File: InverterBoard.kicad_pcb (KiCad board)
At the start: 2 copper layers, 72 x 95 mm, 109 parts, among them J1 PinHeader, J2 5VIN, J3 GateDrivePower, J4 Motor, J5 BrakeResistor, J6 DC_Link, Q1 IPA60R280P7S, Q2 IPA60R280P7S, Q3 IPA60R280P7S, Q4 IPA60R280P7S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

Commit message: アートワークも一応完成
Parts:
- removed the R23 at (-88.9, -2.54)
- removed the R24 at (-85.1, 29.2)
- removed the R24 at (-83.8, 21.6)
- removed the REF** at (33.0, 44.5)
- removed the REF** at (-33.0, 44.5)
- removed the REF** at (33.0, -44.5)
- added R24: 330R, Resistor_SMD:R_0603_1608Metric, B.Cu at (21.0, 19.1)
- added REF**: MountingHole_3.2mm_M3, MountingHole:MountingHole_3.2mm_M3, F.Cu at (44.5, -33.0)
- added REF**: MountingHole_3.2mm_M3, MountingHole:MountingHole_3.2mm_M3, F.Cu at (44.5, 33.0)
- added REF**: MountingHole_3.2mm_M3, MountingHole:MountingHole_3.2mm_M3, F.Cu at (-44.5, -33.0)
- C16, C17, C18, C19, C20, C21, JP1, JP2, R23, R25, R26, R27, R28: moved to B.Cu
- moved C17 127.0 mm to (25.4, 21.0)
- moved R27 123.3 mm to (29.2, 23.5), turned to 90 degrees
- moved C21 122.6 mm to (31.1, 20.3), turned to 90 degrees
- moved R28 119.5 mm to (29.2, 20.3), turned to 90 degrees
- moved JP2 101.7 mm to (25.4, 23.1)
- moved C19 98.6 mm to (21.0, 21.0), turned to 180 degrees
- moved C16 98.1 mm to (-5.08, 26.0)
- moved C1 96.8 mm to (-29.8, 33.0), turned to 270 degrees
- moved JP1 95.4 mm to (-5.08, 28.2)
- moved R23 95.0 mm to (-0.64, 24.1), turned to 180 degrees
- moved R25 89.2 mm to (-6.99, 30.2)
- moved C18 86.8 mm to (-0.64, 26.0), turned to 180 degrees
- moved C20 84.7 mm to (-3.17, 31.8)
- moved D4 84.2 mm to (-27.9, 29.8)
- moved C2 82.1 mm to (-23.5, 33.0), turned to 270 degrees
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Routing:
- net GND: track 2.78 -> 181.4 mm, vias 1 -> 7
- net GNDPWR: track 222.6 -> 401.0 mm, vias 3 -> 6
- net +3V3: track 2.78 -> 124.2 mm, vias 1 -> 2
- net /Sensor/IW-: track 39.8 -> 104.2 mm, vias 1 -> 4
- net /Sensor/IU-: track 44.8 -> 106.1 mm, vias 1 -> 4
- net /GateDrive/GATE_WP: track 0.00 -> 54.8 mm, vias 0 -> 1
- net /GateDrive/GATE_VP: track 0.00 -> 52.4 mm, vias 0 -> 1
- net SIG_BR: track 0.00 -> 51.4 mm
- net /GateDrive/GATE_UP: track 0.00 -> 48.8 mm, vias 0 -> 1
- net /GateDrive/SOURCE_VP: track 67.7 -> 114.3 mm, vias 0 -> 3
- net /GateDrive/GATE_WN: track 0.00 -> 43.5 mm, vias 0 -> 1
- net /GateDrive/GATE_VN: track 0.00 -> 40.7 mm, vias 0 -> 1
- net /GateDrive/GATE_UN: track 0.00 -> 39.1 mm, vias 0 -> 1
- net SEN_IU_REF: track 0.00 -> 38.8 mm
- net SIG_UP: track 0.00 -> 38.5 mm
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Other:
- board size 72 x 95 mm -> 95 x 72 mm
- board text added: "-"
- board text added: "1"
- board text added: "19"
- board text added: "2"
- board text added: "20"
- board text added: "Designed by @akito_0914"
- board text added: "GBR"
- board text added: "GND"
- board text added: "GUN"
- board text added: "GUP"
- board text added: "GVN"
- board text added: "GVP"
- board text added: "GWN"
- board text added: "GWP"
- board text added: "Inverter board"
- board text added: "MOTOR"
- board text added: "MyServoAmpProject"
- board text added: "RES"
- board text added: "SIU"
- board text added: "SIU0"
- board text added: "SIW"
- board text added: "SIW0"
- board text added: "SVDC+"
- board text added: "SVDC-"
- board text added: "VDC"

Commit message: TODO削除
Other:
- board text removed: "TODO: Fix connection from motor line to current sensor."
- board text removed: "TODO: Fix via at current sensor."
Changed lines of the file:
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@@
   (general
     (thickness 1.6)
-    (drawings 121)
+    (drawings 119)
     (tracks 769)
     (zones 0)
@@
   )
   (setup
-    (last_trace_width 1)
+    (last_trace_width 0.25)
     (user_trace_width 0.15)
     (user_trace_width 0.2)
@@
     (arrow2b (pts (xy 0 45.72) (xy 1.126504 45.133579)))
   )
-  (gr_text "TODO: Fix connection from motor line to current sensor." (at 327.66 -109.22) (layer Dwgs.User)
-    (effects (font (size 10 10) (thickness 1.5)))
-  )
-  (gr_text "TODO: Fix via at current sensor." (at 232.41 -128.905) (layer Dwgs.User)
-    (effects (font (size 10 10) (thickness 1.5)))
-  )
   (gr_line (start -27.94 20.32) (end 11.43 20.32) (layer Dwgs.User) (width 0.15))

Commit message: テストポイント追加，シルク調整，固定穴マスク追加
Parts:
- removed REF** (x4): MountingHole_3.2mm_M3, MountingHole:MountingHole_3.2mm_M3
- added H1: MountingHole, MountingHole:MountingHole_3.2mm_M3, F.Cu at (-44.5, -33.0)
- added H2: MountingHole, MountingHole:MountingHole_3.2mm_M3, F.Cu at (44.5, -33.0)
- added H3: MountingHole, MountingHole:MountingHole_3.2mm_M3, F.Cu at (44.5, 33.0)
- added H4: MountingHole, MountingHole:MountingHole_3.2mm_M3, F.Cu at (-44.5, 33.0)
- added TP1: TestPoint, TestPoint:TestPoint_Loop_D2.50mm_Drill1.0mm_LowProfile, F.Cu at (-41.9, 27.9)
- added TP10: TestPoint, TestPoint:TestPoint_Pad_D1.0mm, F.Cu at (-5.08, 27.3)
- added TP11: TestPoint, TestPoint:TestPoint_Pad_D1.0mm, F.Cu at (0.00, 27.3)
- added TP12: TestPoint, TestPoint:TestPoint_Pad_D1.0mm, F.Cu at (5.08, 27.3)
- added TP13: TestPoint, TestPoint:TestPoint_Loop_D2.50mm_Drill1.0mm_LowProfile, F.Cu at (-33.0, -29.8)
- added TP14: TestPoint, TestPoint:TestPoint_Loop_D2.50mm_Drill1.0mm_LowProfile, F.Cu at (-38.7, -33.0)
- added TP15: TestPoint, TestPoint:TestPoint_Loop_D2.50mm_Drill1.0mm_LowProfile, F.Cu at (-28.6, -5.71)
- added TP16: TestPoint, TestPoint:TestPoint_Loop_D2.50mm_Drill1.0mm_LowProfile, F.Cu at (-5.08, -9.50)
- added TP17: TestPoint, TestPoint:TestPoint_Loop_D2.50mm_Drill1.0mm_LowProfile, F.Cu at (10.2, -9.53)
- added TP18: TestPoint, TestPoint:TestPoint_Loop_D2.50mm_Drill1.0mm_LowProfile, F.Cu at (25.4, -9.50)
- added TP19: TestPoint, TestPoint:TestPoint_Pad_D1.0mm, B.Cu at (0.00, 27.9)
- added TP2: TestPoint, TestPoint:TestPoint_Loop_D2.50mm_Drill1.0mm_LowProfile, F.Cu at (-19.7, 33.0)
- added TP20: TestPoint, TestPoint:TestPoint_Pad_D1.0mm, B.Cu at (21.6, 22.9)
- added TP21: TestPoint, TestPoint:TestPoint_Pad_D1.0mm, B.Cu at (-5.71, 32.4)
- added TP22: TestPoint, TestPoint:TestPoint_Pad_D1.0mm, B.Cu at (31.8, 22.9)
- added TP23: TestPoint, TestPoint:TestPoint_Pad_D1.0mm, F.Cu at (45.7, 8.89)
- added TP24: TestPoint, TestPoint:TestPoint_Loop_D2.50mm_Drill1.0mm_LowProfile, F.Cu at (36.8, 12.1)
- added TP25: TestPoint, TestPoint:TestPoint_Pad_D1.0mm, F.Cu at (37.5, 23.5)
- added TP26: TestPoint, TestPoint:TestPoint_Pad_D1.0mm, F.Cu at (37.5, 20.3)
- added TP3: TestPoint, TestPoint:TestPoint_Loop_D2.50mm_Drill1.0mm_LowProfile, F.Cu at (-45.1, 24.8)
- added TP4: TestPoint, TestPoint:TestPoint_Loop_D2.50mm_Drill1.0mm_LowProfile, F.Cu at (-36.8, 12.1)
- added TP5: TestPoint, TestPoint:TestPoint_Pad_D1.0mm, F.Cu at (45.7, -1.91)
- added TP6: TestPoint, TestPoint:TestPoint_Pad_D1.0mm, F.Cu at (-20.3, 27.3)
- added TP7: TestPoint, TestPoint:TestPoint_Pad_D1.0mm, F.Cu at (-15.2, 27.3)
- added TP8: TestPoint, TestPoint:TestPoint_Pad_D1.0mm, F.Cu at (-25.4, 27.3)
- added TP9: TestPoint, TestPoint:TestPoint_Pad_D1.0mm, F.Cu at (-10.2, 27.3)
- C24: moved to F.Cu
- C25, R41, R42: moved to B.Cu
- J1: footprint Connector_PinHeader_2.54mm:PinHeader_2x10_P2.54mm_Vertical -> Connector_IDC:IDC-Header_2x10_P2.54mm_Vertical
- moved D1 7.41 mm to (-22.2, 29.8), turned to 90 degrees
- moved R1 6.87 mm to (-24.8, 29.8)
- moved R41 3.86 mm to (36.2, 26.7), turned to 270 degrees
- moved D2 3.18 mm to (-33.0, 14.0)
- moved C7 2.54 mm to (-27.9, 16.3)
- moved D7 2.54 mm to (-27.9, 11.7)
- moved R11 2.54 mm to (-27.9, 26.9)
- moved R14 2.54 mm to (-27.9, 14.6)
- moved R3 2.54 mm to (-23.5, -33.0)
- moved U4 2.54 mm to (-27.9, 21.6)
- moved C6 2.54 mm to (-17.8, 16.3)
- moved D8 2.54 mm to (-17.8, 11.7)
- moved R10 2.54 mm to (-17.8, 26.9)
- moved R13 2.54 mm to (-17.8, 14.6)
- moved U3 2.54 mm to (-17.8, 21.6)
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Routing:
- net GNDPWR: track 401.0 -> 422.5 mm
- net GND: track 181.4 -> 199.9 mm, vias 7 -> 9
- net /Sensor/IW-: track 104.2 -> 116.5 mm
- net /Sensor/IU-: track 106.1 -> 117.0 mm
- net SEN_VDC_N: track 8.78 -> 18.6 mm, vias 0 -> 1
- net +5VP: track 6.43 -> 15.7 mm
- net Net-(C22-Pad1): track 12.7 -> 20.5 mm
- net /GateDrive/GATE_WP: track 54.8 -> 61.0 mm
- net Net-(R41-Pad2): track 6.85 -> 13.0 mm, vias 0 -> 1
- net /GateDrive/SOURCE_VP: track 114.3 -> 120.1 mm
- net SEN_VDC_P: track 10.7 -> 16.0 mm, vias 0 -> 1
- net /MainCircuit/BR_L: track 32.9 -> 38.1 mm
- net SIG_VN: track 26.1 -> 31.1 mm
- net SIG_VP: track 33.6 -> 38.5 mm
- net SIG_WP: track 24.9 -> 29.8 mm
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
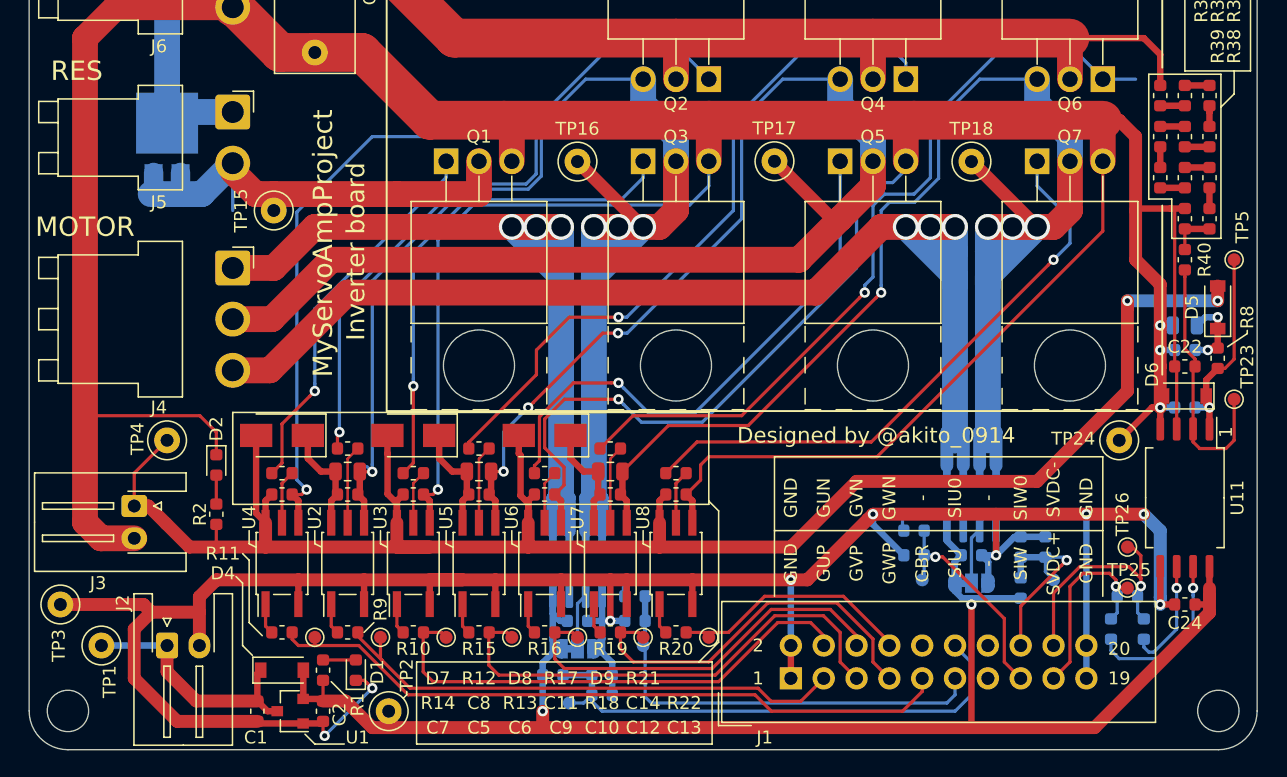
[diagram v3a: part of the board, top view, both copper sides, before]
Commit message: GNDベタ追加，電流センサ周辺部品の配置調整
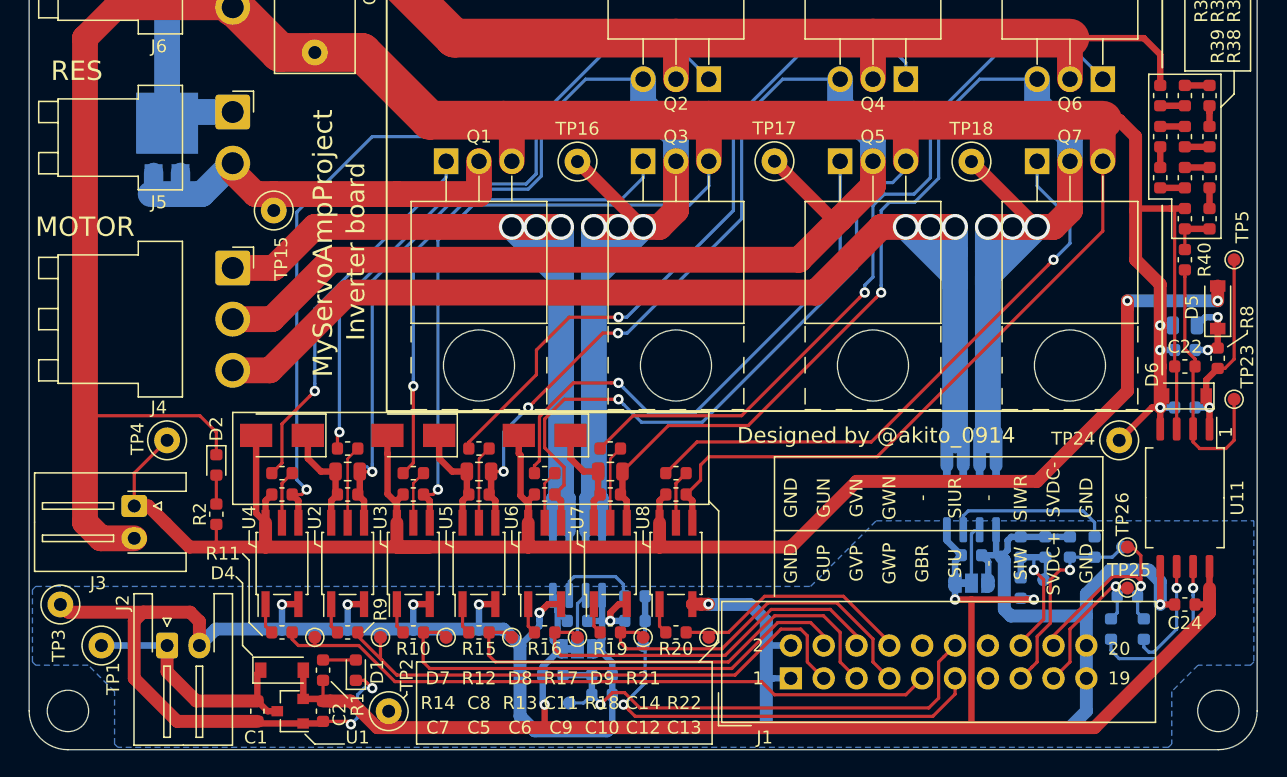
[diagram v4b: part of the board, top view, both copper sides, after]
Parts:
- moved TP20 15.7 mm to (37.1, 20.3)
- moved R24 14.0 mm to (34.9, 20.3), turned to 90 degrees
- moved C19 12.1 mm to (33.0, 20.3), turned to 90 degrees
- moved TP22 0.76 mm to (31.0, 22.9)
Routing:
- net GND: track 199.9 -> 216.6 mm, vias 9 -> 10
- net Net-(R24-Pad2): track 7.22 -> 12.9 mm
- net /MainCircuit/BR_L: track 38.1 -> 34.5 mm
- net SEN_IU: track 35.5 -> 39.0 mm, vias 0 -> 1
- net SEN_VDC_P: track 16.0 -> 13.0 mm
- net SIG_UP: track 41.3 -> 43.9 mm
- net /GateDrive/GATE_WP: track 61.0 -> 58.5 mm
- net SEN_VDC_N: track 18.6 -> 16.1 mm
- net SEN_IW_REF: track 15.3 -> 13.2 mm
- net SEN_IU_REF: track 40.8 -> 38.8 mm, vias 0 -> 1
- net SIG_BR: track 53.9 -> 52.2 mm
- net SEN_IW: track 17.3 -> 15.8 mm
- net SIG_UN: track 39.3 -> 38.1 mm
- net SIG_VN: track 31.1 -> 29.8 mm
- net SIG_VP: track 38.5 -> 37.2 mm
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- added copper zone on B.Cu, net GND
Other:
- board text added: "SIUR"
- board text added: "SIWR"
- board text removed: "SIU0"
- board text removed: "SIW0"

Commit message: 配線ちょっと修正
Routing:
- net /GateDrive/GATE_VP: track 53.5 -> 52.3 mm
- net /GateDrive/GATE_WN: track 46.0 -> 46.9 mm
- net GNDPWR: track 422.5 -> 423.1 mm
